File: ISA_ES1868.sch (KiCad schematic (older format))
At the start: 14 parts, among them J1 ISA BUS, U1 L78L05_TO92, U4 93LC66

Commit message: More schematics
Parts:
- added C13: 10uF, Capacitor_THT:CP_Radial_D5.0mm_P2.50mm, symbol Device:CP_Small
- added R1, R2: 7.5k, symbol Device:R_Small
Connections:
- net GNDA: now also C13.2
- net at C12.1, C5.1, U1.1 (VO)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: now also R1.1
- new net: C13.1, R1.2, R2.1
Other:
- moved on the sheet: C4, U1
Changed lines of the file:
@@
 	13100 4750 13100 4800
 Wire Wire Line
-	12650 4050 12650 4100
-Connection ~ 12650 4050
-Wire Wire Line
-	13300 4050 13300 4000
-Wire Wire Line
-	12650 4050 13300 4050
-Wire Wire Line
-	12650 4000 12650 4050
-$Comp
-L power:GNDA #PWR?
-U 1 1 60AE9C0E
-P 12650 4100
-F 0 "#PWR?" H 12650 3850 50  0001 C CNN
-F 1 "GNDA" H 12800 4050 50  0000 C CNN
-F 2 "" H 12650 4100 50  0001 C CNN
-F 3 "" H 12650 4100 50  0001 C CNN
-	1    12650 4100
-	1    0    0    -1
-$EndComp
-Wire Wire Line
-	12650 3700 13000 3700
-Connection ~ 12650 3700
-Wire Wire Line
-	12650 3700 12650 3800
-Wire Wire Line
-	12400 3700 12650 3700
-Wire Wire Line
-	12400 3650 12400 3700
-$Comp
-L power:+12V #PWR?
-U 1 1 60AD7461
-P 12400 3650
-F 0 "#PWR?" H 12400 3500 50  0001 C CNN
-F 1 "+12V" H 12250 3700 50  0000 C CNN
-F 2 "" H 12400 3650 50  0001 C CNN
-F 3 "" H 12400 3650 50  0001 C CNN
-	1    12400 3650
-	1    0    0    -1
-$EndComp
-$Comp
-L Device:C_Small C4
-U 1 1 60ACF5FB
-P 12650 3900
-F 0 "C4" H 12742 3946 50  0000 L CNN
-F 1 "100nF" H 12742 3855 50  0000 L CNN
-F 2 "Capacitor_THT:C_Disc_D6.0mm_W2.5mm_P5.00mm" H 12650 3900 50  0001 C CNN
-F 3 "~" H 12650 3900 50  0001 C CNN
-	1    12650 3900
-	1    0    0    -1
-$EndComp
-$Comp
-L Regulator_Linear:L78L05_TO92 U1
-U 1 1 60ACA4DD
-P 13300 3700
-F 0 "U1" H 13300 3942 50  0000 C CNN
-F 1 "L78L05_TO92" H 13300 3851 50  0000 C CNN
-F 2 "Package_TO_SOT_THT:TO-92_Inline" H 13300 3925 50  0001 C CIN
-F 3 "http://www.st.com/content/ccc/resource/technical/document/datasheet/15/55/e5/aa/23/5b/43/fd/CD00000446.pdf/files/CD00000446.pdf/jcr:content/translations/en.CD00000446.pdf" H 13300 3650 50  0001 C CNN
-	1    13300 3700
-	1    0    0    -1
-$EndComp
-$Comp
-L custom_components:ES1868F U?
-U 1 1 60A9AA6E
-P 11850 7150
-F 0 "U?" H 11400 10050 50  0000 C CNN
-F 1 "ES1868F" H 12200 10050 50  0000 C CNN
-F 2 "" H 11850 8100 50  0001 C CNN
-F 3 "" H 11850 8100 50  0001 C CNN
-	1    11850 7150
-	1    0    0    -1
-$EndComp
-Wire Wire Line
 	12450 4550 12700 4550
-Wire Wire Line
-	13700 4550 13700 3700
-Wire Wire Line
-	13700 3700 13600 3700
 $Comp
 L Device:C_Small C5
@@
 	1    0    0    -1
 $EndComp
-Connection ~ 13150 4550
-Wire Wire Line
-	13150 4550 13700 4550
 Wire Wire Line
 	13100 4750 13150 4750
 Connection ~ 13100 4750
+$Comp
+L Device:R_Small R1
+U 1 1 60B14C7D
+P 13800 4550
+F 0 "R1" V 13900 4500 50  0000 L CNN
+F 1 "7.5k" V 13700 4450 50  0000 L CNN
+F 2 "" H 13800 4550 50  0001 C CNN
+F 3 "~" H 13800 4550 50  0001 C CNN
+	1    13800 4550
+	0    -1   -1   0
+$EndComp
+Wire Wire Line
+	13550 3700 13450 3700
+$Comp
+L custom_components:ES1868F U?
+U 1 1 60A9AA6E
+P 11850 7150
+F 0 "U?" H 11400 10050 50  0000 C CNN
+F 1 "ES1868F" H 12200 10050 50  0000 C CNN
+F 2 "" H 11850 8100 50  0001 C CNN
+F 3 "" H 11850 8100 50  0001 C CNN
+	1    11850 7150
+	1    0    0    -1
+$EndComp
+$Comp
+L Regulator_Linear:L78L05_TO92 U1
+U 1 1 60ACA4DD
+P 13150 3700
+F 0 "U1" H 13150 3942 50  0000 C CNN
+F 1 "L78L05_TO92" H 13150 3851 50  0000 C CNN
+F 2 "Package_TO_SOT_THT:TO-92_Inline" H 13150 3925 50  0001 C CIN
+F 3 "http://www.st.com/content/ccc/resource/technical/document/datasheet/15/55/e5/aa/23/5b/43/fd/CD00000446.pdf/files/CD00000446.pdf/jcr:content/translations/en.CD00000446.pdf" H 13150 3650 50  0001 C CNN
+	1    13150 3700
+	1    0    0    -1
+$EndComp
+$Comp
+L Device:C_Small C4
+U 1 1 60ACF5FB
+P 12500 3900
+F 0 "C4" H 12592 3946 50  0000 L CNN
+F 1 "100nF" H 12592 3855 50  0000 L CNN
+F 2 "Capacitor_THT:C_Disc_D6.0mm_W2.5mm_P5.00mm" H 12500 3900 50  0001 C CNN
+F 3 "~" H 12500 3900 50  0001 C CNN
+	1    12500 3900
+	1    0    0    -1
+$EndComp
+$Comp
+L power:+12V #PWR?
+U 1 1 60AD7461
+P 12250 3650
+F 0 "#PWR?" H 12250 3500 50  0001 C CNN
+F 1 "+12V" H 12100 3700 50  0000 C CNN
+F 2 "" H 12250 3650 50  0001 C CNN
+F 3 "" H 12250 3650 50  0001 C CNN
+	1    12250 3650
+	1    0    0    -1
+$EndComp
+Wire Wire Line
+	12250 3650 12250 3700
+Wire Wire Line
+	12250 3700 12500 3700
+Wire Wire Line
+	12500 3700 12500 3800
+Connection ~ 12500 3700
+Wire Wire Line
+	12500 3700 12850 3700
+$Comp
+L power:GNDA #PWR?
+U 1 1 60AE9C0E
+P 12500 4100
+F 0 "#PWR?" H 12500 3850 50  0001 C CNN
+F 1 "GNDA" H 12650 4050 50  0000 C CNN
+F 2 "" H 12500 4100 50  0001 C CNN
+F 3 "" H 12500 4100 50  0001 C CNN
+	1    12500 4100
+	1    0    0    -1
+$EndComp
+Wire Wire Line
+	12500 4000 12500 4050
+Wire Wire Line
+	12500 4050 13150 4050
+Wire Wire Line
+	13150 4050 13150 4000
+Connection ~ 12500 4050
+Wire Wire Line
+	12500 4050 12500 4100
+Wire Wire Line
+	13550 3700 13550 4550
+Wire Wire Line
+	13550 4550 13150 4550
+Connection ~ 13150 4550
+Wire Wire Line
+	13700 4550 13550 4550
+Connection ~ 13550 4550
+$Comp
+L Device:CP_Small C13
+U 1 1 60B35976
+P 14100 4650
+F 0 "C13" H 14188 4696 50  0000 L CNN
+F 1 "10uF" H 14188 4605 50  0000 L CNN
+F 2 "Capacitor_THT:CP_Radial_D5.0mm_P2.50mm" H 14100 4650 50  0001 C CNN
+F 3 "~" H 14100 4650 50  0001 C CNN
+	1    14100 4650
+	1    0    0    -1
+$EndComp
+Wire Wire Line
+	13900 4550 14100 4550
+$Comp
+L power:GNDA #PWR?
+U 1 1 60B3A27D
+P 14100 4750
+F 0 "#PWR?" H 14100 4500 50  0001 C CNN
+F 1 "GNDA" H 14250 4700 50  0000 C CNN
+F 2 "" H 14100 4750 50  0001 C CNN
+F 3 "" H 14100 4750 50  0001 C CNN
+	1    14100 4750
+	1    0    0    -1
+$EndComp
+$Comp
+L Device:R_Small R2
+U 1 1 60B3ACBC
+P 14500 4550
+F 0 "R2" V 14600 4500 50  0000 L CNN
+F 1 "7.5k" V 14400 4450 50  0000 L CNN
+F 2 "" H 14500 4550 50  0001 C CNN
+F 3 "~" H 14500 4550 50  0001 C CNN
+	1    14500 4550
+	0    -1   -1   0
+$EndComp
+Wire Wire Line
+	14100 4550 14400 4550
+Connection ~ 14100 4550
 $EndSCHEMATC

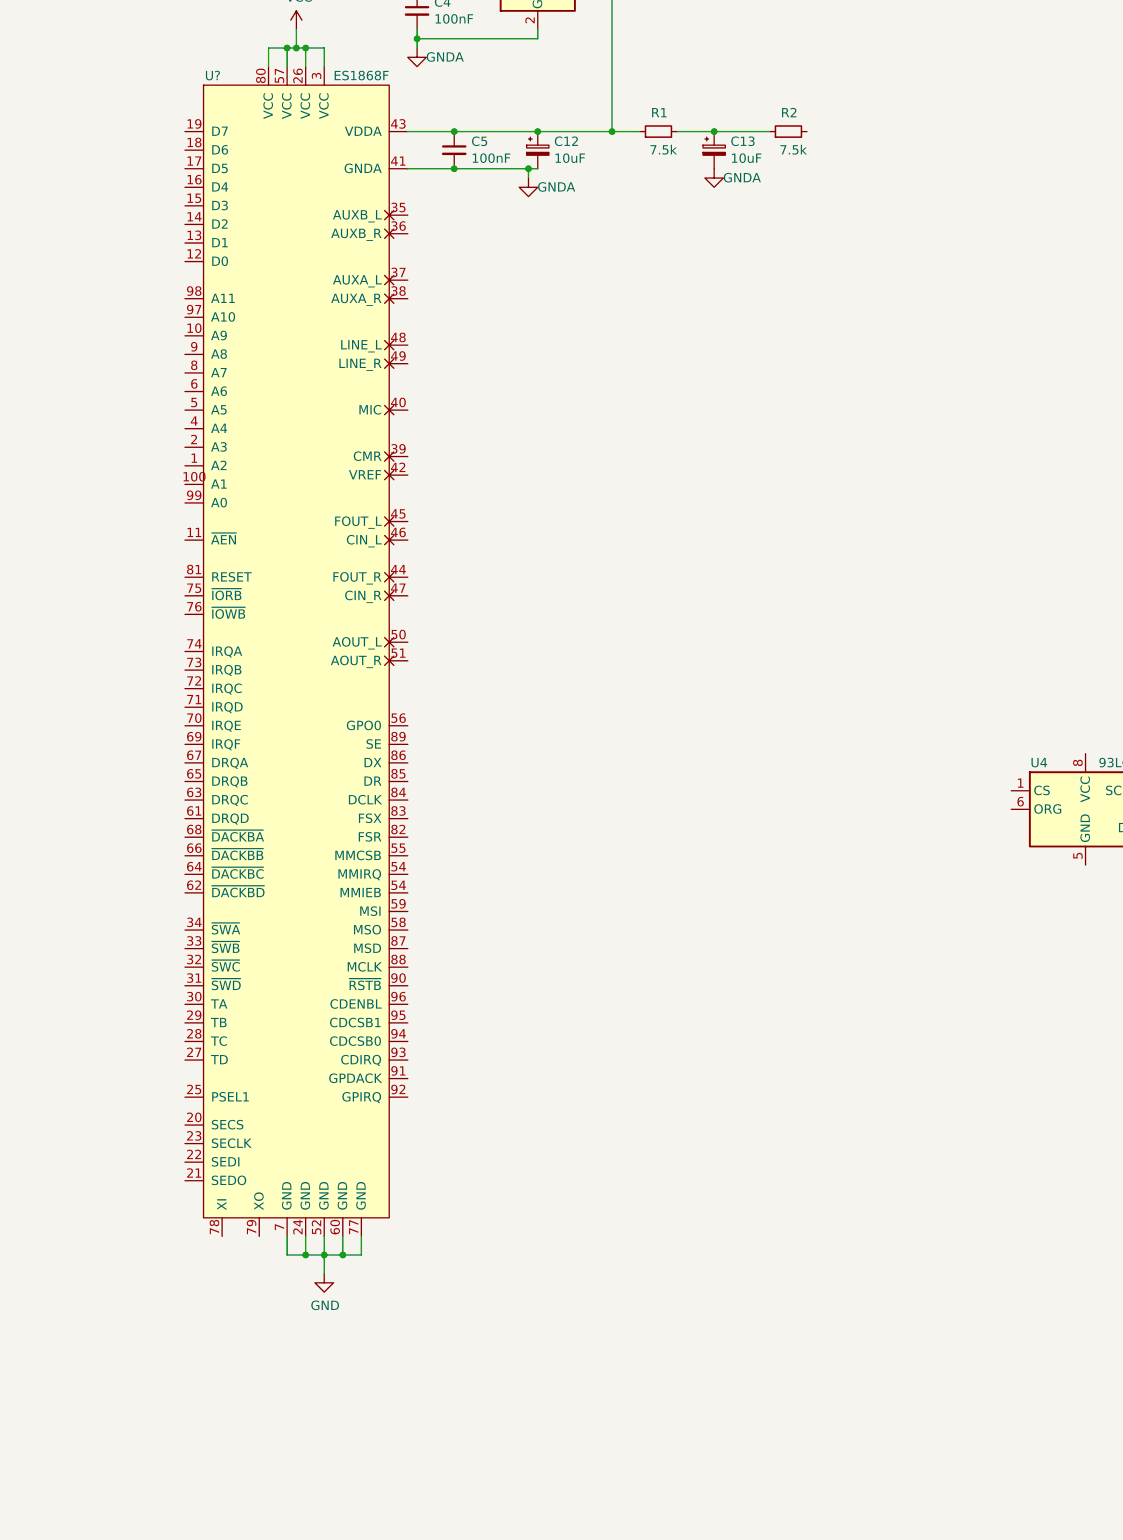
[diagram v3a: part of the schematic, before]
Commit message: Copy over more of the schematics for the audio chip
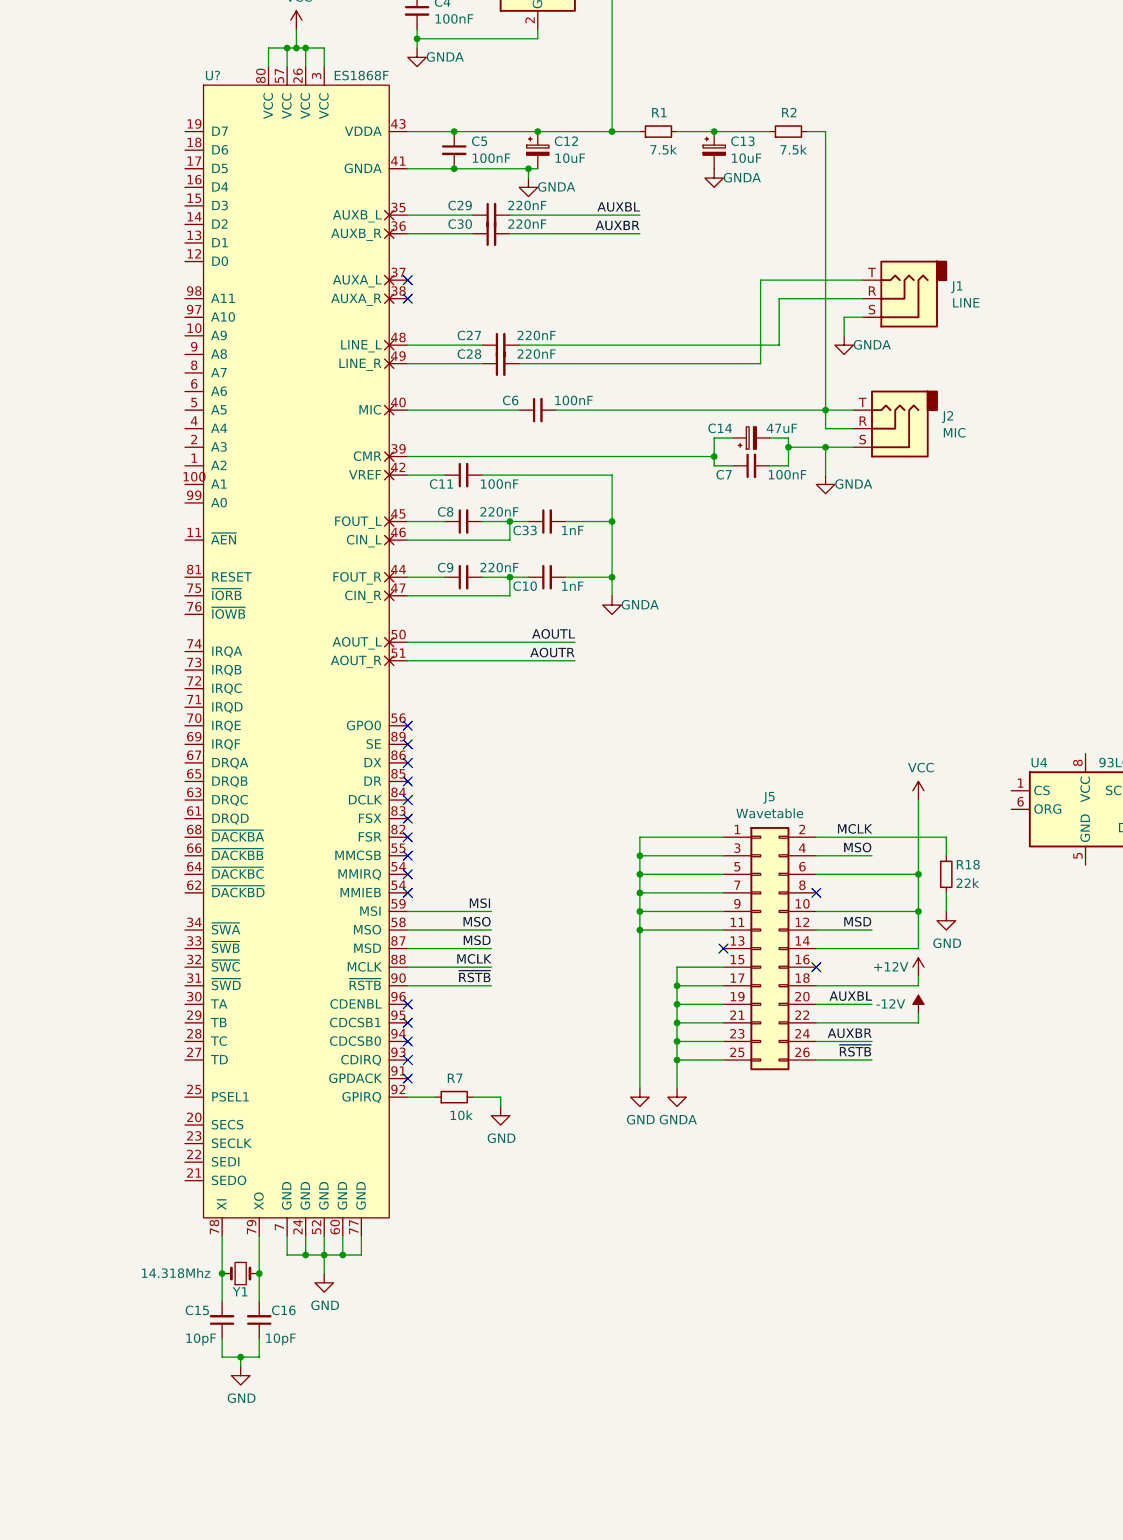
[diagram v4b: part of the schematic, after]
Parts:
- added C10, C33: 1nF, Capacitor_THT:C_Disc_D6.0mm_W2.5mm_P5.00mm, symbol Device:C_Small
- added C11, C6, C7: 100nF, Capacitor_THT:C_Disc_D6.0mm_W2.5mm_P5.00mm, symbol Device:C_Small
- added C14: 47uF, Capacitor_THT:CP_Radial_D5.0mm_P2.50mm, symbol Device:CP_Small
- added C15, C16: 10pF, Capacitor_THT:C_Disc_D6.0mm_W2.5mm_P5.00mm, symbol Device:C_Small
- added C27, C28, C29, C30, C8, C9: 220nF, Capacitor_THT:C_Disc_D6.0mm_W2.5mm_P5.00mm, symbol Device:C_Small
- added J1: LINE, symbol Connector:AudioJack3
- added J2: MIC, symbol Connector:AudioJack3
- added J5: Wavetable, symbol Connector_Generic:Conn_02x13_Odd_Even
- added R18: 22k, symbol Device:R_Small
- added R7: 10k, symbol Device:R_Small
- added Y1: 14.318Mhz, symbol Device:Crystal_Small
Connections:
- net +12V: now also J5.18 (Pin_18)
- net -12V: now also J5.22 (Pin_22)
- net GND: now also C15.1, C16.1, J5.1 (Pin_1), J5.11 (Pin_11), J5.3 (Pin_3), J5.5 (Pin_5), J5.7 (Pin_7), J5.9 (Pin_9), R18.2, R7.2
- net GNDA: now also C10.2, C11.2, C14.2, C33.2, C7.2, J1.S, J2.S, J5.15 (Pin_15), J5.17 (Pin_17), J5.19 (Pin_19), J5.21 (Pin_21), J5.23 (Pin_23), J5.25 (Pin_25)
- net VCC: now also J5.10 (Pin_10), J5.14 (Pin_14), J5.6 (Pin_6)
- net at U?.35 (AUXB_L): now also C29.1
- net at U?.36 (AUXB_R): now also C30.1
- net at U?.39 (CMR): now also C14.1, C7.1
- net at U?.40 (MIC): now also C6.1
- net at U?.42 (VREF): now also C11.1
- net at U?.44 (FOUT_R): now also C9.1
- net at U?.45 (FOUT_L): now also C8.1
- net at U?.46 (CIN_L): now also C33.1, C8.2
- net at U?.47 (CIN_R): now also C10.1, C9.2
- net at U?.48 (LINE_L): now also C27.1
- net at U?.49 (LINE_R): now also C28.1
- net AOUTL: now reaches U?.50 (AOUT_L)
- net AOUTR: now reaches U?.51 (AOUT_R)
- net MSO: now reaches U?.58 (MSO)
- net MSO: now also J5.4 (Pin_4)
- net MSI: now reaches U?.59 (MSI)
- net at U?.78 (XI): now also C15.2, Y1.1
- net at U?.79 (XO): now also C16.2, Y1.2
- net MSD: now reaches U?.87 (MSD)
- net MSD: now also J5.12 (Pin_12)
- net MCLK: now reaches U?.88 (MCLK)
- net MCLK: now also J5.2 (Pin_2), R18.1
- net ~RSTB: now reaches U?.90 (~RSTB)
- net ~RSTB: now also J5.26 (Pin_26)
- net at U?.92 (GPIRQ): now also R7.1
- net at R2.2: now also C6.2, J2.R, J2.T
- new net: C27.2, J1.R
- new net: C28.2, J1.T
- new net AUXBL: C29.2, J5.20 (Pin_20)
- new net AUXBR: C30.2, J5.24 (Pin_24)
- no-connect marks 13 -> 33

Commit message: More schematics
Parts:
- added C46: 1nF, Capacitor_THT:C_Disc_D6.0mm_W2.5mm_P5.00mm, symbol Device:C_Small
- added J3: Joystick/MIDI, symbol Connector:DB15_Female_MountingHoles
- added JP1: IRQ3 Jumper, Jumper:SolderJumper-2_P1.3mm_Open_RoundedPad1.0x1.5mm, symbol Device:Jumper_NO_Small
- added JP2: IRQ4 Jumper, Jumper:SolderJumper-2_P1.3mm_Open_RoundedPad1.0x1.5mm, symbol Device:Jumper_NO_Small
- added JP3: ~DRQ2~ Jumper, Jumper:SolderJumper-2_P1.3mm_Open_RoundedPad1.0x1.5mm, symbol Device:Jumper_NO_Small
- added JP4: ~DACK2~ Jumper, Jumper:SolderJumper-2_P1.3mm_Open_RoundedPad1.0x1.5mm, symbol Device:Jumper_NO_Small
- added U2: 74LS138, symbol 74xx:74LS138
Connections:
- net A0: now also U?.99 (A0)
- net A1: now also U?.100 (A1)
- net A10: now also U?.97 (A10)
- net A11: now also U?.98 (A11)
- net A12: now also U2.4 (E1)
- net A13: now also U2.3 (A2)
- net A14: now also U2.2 (A1)
- net A15: now also U2.1 (A0)
- net A2: now also U?.1 (A2)
- net A3: now also U?.2 (A3)
- net A4: now also U?.4 (A4)
- net A5: now also U?.5 (A5)
- net A6: now also U?.6 (A6)
- net A7: now also U?.8 (A7)
- net A8: now also U?.9 (A8)
- net A9: now also U?.10 (A9)
- net AEN: now also U2.5 (E2)
- net D0: now also U?.12 (D0)
- net D1: now also U?.13 (D1)
- net D2: now also U?.14 (D2)
- net D3: now also U?.15 (D3)
- net D4: now also U?.16 (D4)
- net D5: now also U?.17 (D5)
- net D6: now also U?.18 (D6)
- net D7: now also U?.19 (D7)
- net DRQ1: now also U?.65 (DRQB)
- net DRQ2: now also JP3.1
- net DRQ3: now also U?.63 (DRQC)
- net GND: now also C46.1, J3.0 (PAD), U2.8 (GND)
- net IRQ3: now also JP1.1
- net IRQ4: now also JP2.1
- net IRQ5: now also U?.73 (IRQB)
- net IRQ7: now also U?.72 (IRQC)
- net IRQ9: now also U?.74 (IRQA)
- net RESETDRV: now also U?.81 (RESET), C46.2
- net VCC: now also U2.16 (VCC), U2.6 (E3)
- net ~DACK1: now also U?.66 (~DACKBB)
- net ~DACK2: now also JP4.1
- net ~DACK3: now also U?.64 (~DACKBC)
- net ~IOR: now also U?.75 (~IORB)
- net ~IOW: now also U?.76 (~IOWB)
- net at U?.11 (~AEN): now also U2.15 (O0)
- net at U?.67 (DRQA): now also JP3.2
- net at U?.68 (~DACKBA): now also JP4.2
- net at U?.70 (IRQE): now also JP2.2
- net at U?.71 (IRQD): now also JP1.2
- net ~DACK0: no longer names the net of J1.19 (~DACK0)
- no-connect marks 33 -> 44
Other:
- moved on the sheet: U4
